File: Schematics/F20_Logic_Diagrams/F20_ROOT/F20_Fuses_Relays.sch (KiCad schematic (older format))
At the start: 11 parts, among them K1 MicroRelay, K2 MicroRelay, K3 MicroRelay, K4 MicroRelay, K5 MicroRelay

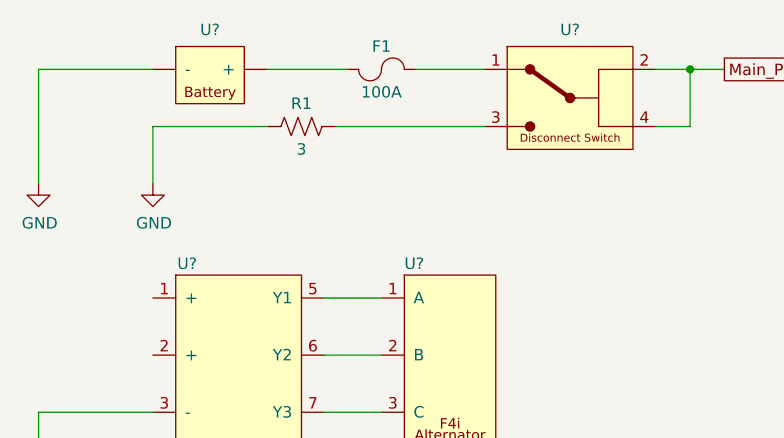
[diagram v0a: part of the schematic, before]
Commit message: Added Driver Display schematic. Added relevant symbols.
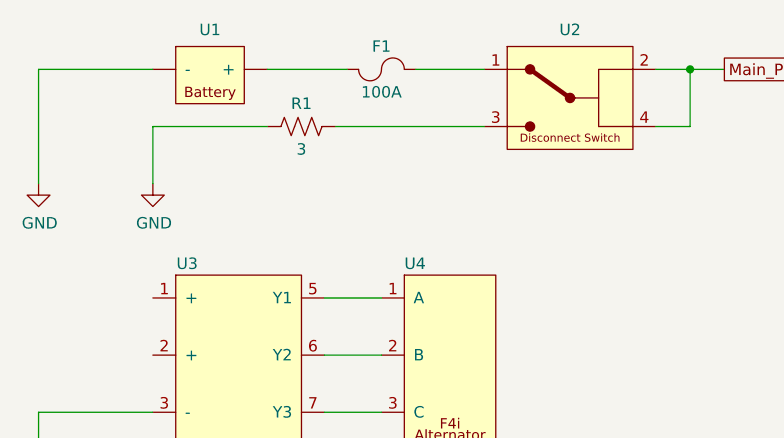
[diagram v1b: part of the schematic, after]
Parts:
- gave numbers to parts that had none: 4
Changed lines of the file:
@@
 EESchema Schematic File Version 4
-LIBS:F20_ROOT-cache
 EELAYER 30 0
 EELAYER END
 $Descr A 11000 8500
 encoding utf-8
-Sheet 2 4
+Sheet 2 5
 Title "Fuses and Relays"
 Date ""
@@
 	7250 1300 7250 2050
 $Comp
-L FSAE_Library:Rectifier U?
+L FSAE_Library:Rectifier U3
 U 1 1 5E21334A
 P 1500 2500
-F 0 "U?" H 1650 2650 50  0000 C CNN
+F 0 "U3" H 1650 2650 50  0000 C CNN
 F 1 "Rectifier" H 1750 2650 50  0001 C CNN
 F 2 "" H 2000 3000 50  0001 C CNN
@@
 $EndComp
 $Comp
-L FSAE_Library:Alternator U?
+L FSAE_Library:Alternator U4
 U 1 1 5E21541A
 P 2500 2500
-F 0 "U?" H 2600 2650 50  0000 L CNN
+F 0 "U4" H 2600 2650 50  0000 L CNN
 F 1 "Alternator" H 2800 2650 50  0001 C CNN
 F 2 "" H 2800 2650 50  0001 C CNN
@@
 Connection ~ 1000 3250
 $Comp
-L FSAE_Library:Battery U?
+L FSAE_Library:Battery U1
 U 1 1 5E233AF7
 P 2000 1500
-F 0 "U?" H 1750 1673 50  0000 C CNN
+F 0 "U1" H 1750 1673 50  0000 C CNN
 F 1 "Battery" H 1750 1650 50  0001 C CNN
 F 2 "" H 1750 1650 50  0001 C CNN
@@
 	1000 1500 1500 1500
 $Comp
-L FSAE_Library:Cutoff_Switch U?
+L FSAE_Library:Cutoff_Switch U2
 U 1 1 5E237569
 P 2950 1500
-F 0 "U?" H 3325 1673 50  0000 C CNN
+F 0 "U2" H 3325 1673 50  0000 C CNN
 F 1 "Cutoff_Switch" H 3300 1650 50  0001 C CNN
 F 2 "" H 3300 1650 50  0001 C CNN

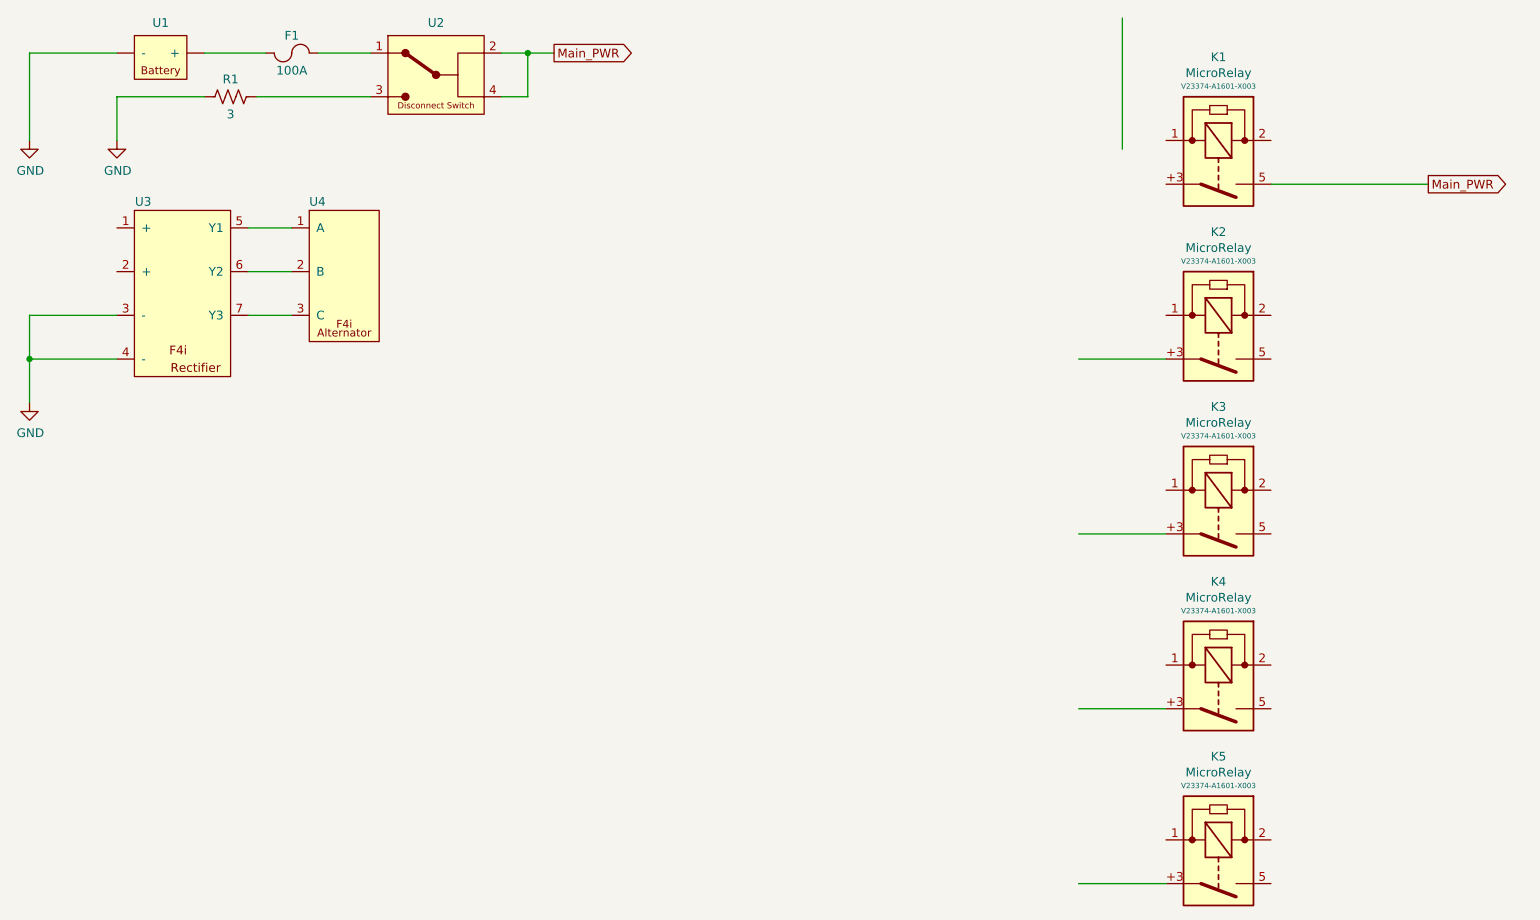
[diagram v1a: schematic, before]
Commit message: Added Brakes logic diagram draft, finished charging/starting schematic portion, added relevant library parts, updated README.
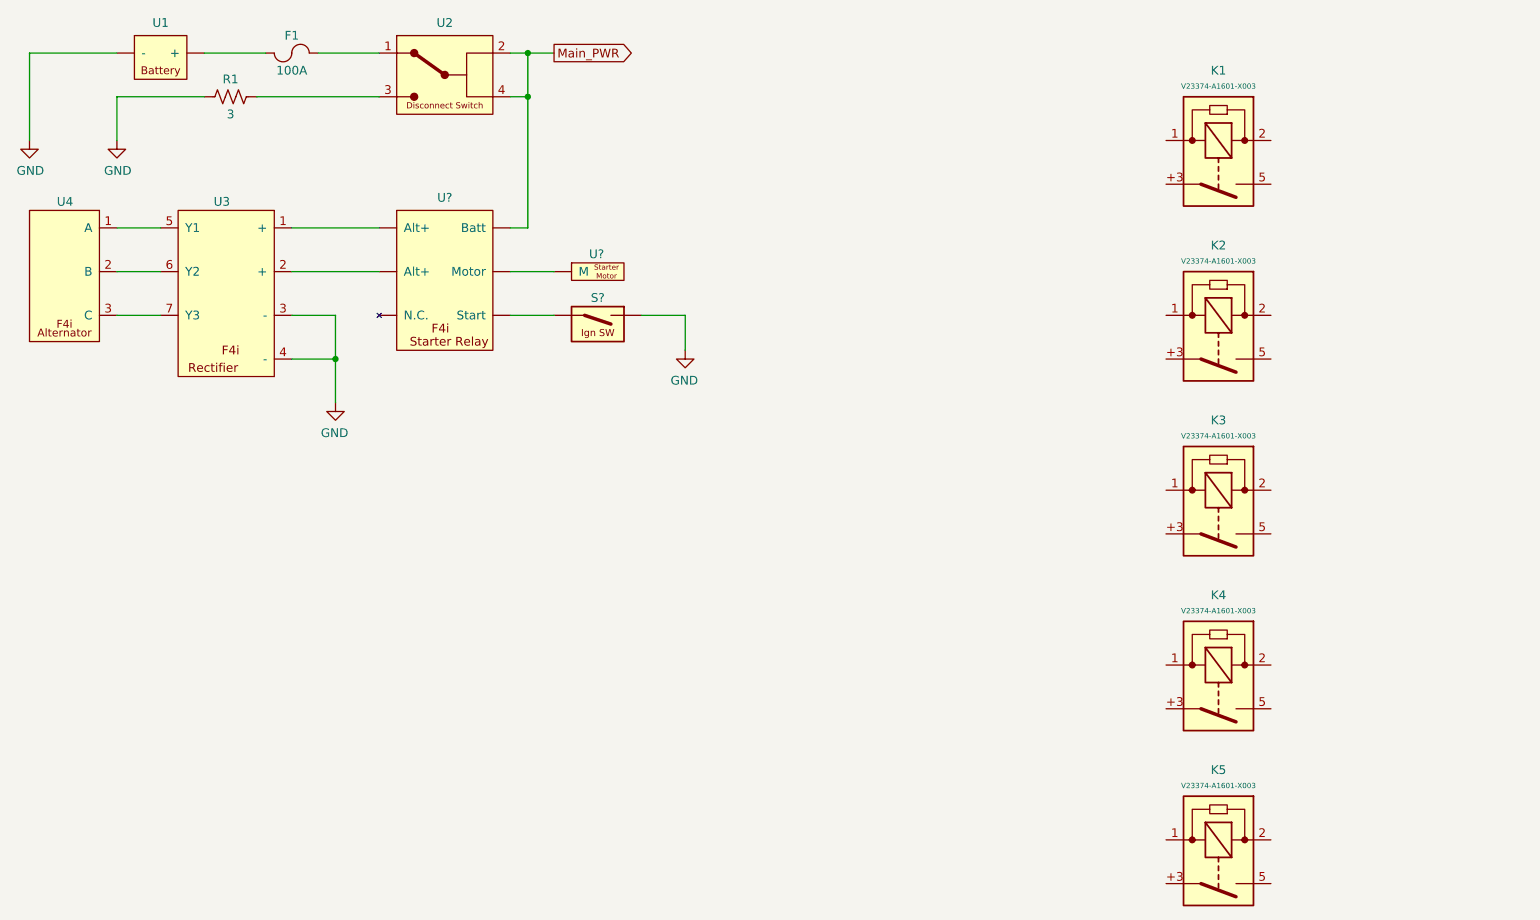
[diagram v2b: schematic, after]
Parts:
- added S?: Ignition_SW, symbol FSAE_Library:Ignition_SW
- added U?: Starter_Relay, symbol FSAE_Library:Starter_Relay
- added U?: Starter_Motor, symbol FSAE_Library:Starter_Motor
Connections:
- wire segments 24 -> 26
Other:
- moved on the sheet: U2, U3, U4
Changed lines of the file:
@@
 EESchema Schematic File Version 4
+LIBS:F20_ROOT-cache
 EELAYER 30 0
 EELAYER END
 $Descr A 11000 8500
 encoding utf-8
-Sheet 2 5
+Sheet 2 6
 Title "Fuses and Relays"
-Date ""
+Date "2020-01-28"
 Rev "A"
 Comp "F20"
@@
 U 1 1 5E20642A
 P 7500 2000
-F 0 "K1" H 7800 2477 50  0000 C CNN
-F 1 "MicroRelay" H 7800 2386 50  0000 C CNN
+F 0 "K1" H 7800 2400 50  0000 C CNN
+F 1 "MicroRelay" H 7800 2386 50  0001 C CNN
 F 2 "" H 7600 1450 50  0001 L CNN
 F 3 "https://www.waytekwire.com/item/75530/MICRO-RELAY-M3-12V-SPST-30A/" V 7800 1800 50  0001 C CNN
@@
 U 1 1 5E207459
 P 7500 3000
-F 0 "K2" H 7800 3477 50  0000 C CNN
-F 1 "MicroRelay" H 7800 3386 50  0000 C CNN
+F 0 "K2" H 7800 3400 50  0000 C CNN
+F 1 "MicroRelay" H 7800 3386 50  0001 C CNN
 F 2 "" H 7600 2450 50  0001 L CNN
 F 3 "https://www.waytekwire.com/item/75530/MICRO-RELAY-M3-12V-SPST-30A/" V 7800 2800 50  0001 C CNN
@@
 U 1 1 5E2083D6
 P 7500 4000
-F 0 "K3" H 7800 4477 50  0000 C CNN
-F 1 "MicroRelay" H 7800 4386 50  0000 C CNN
+F 0 "K3" H 7800 4400 50  0000 C CNN
+F 1 "MicroRelay" H 7800 4386 50  0001 C CNN
 F 2 "" H 7600 3450 50  0001 L CNN
 F 3 "https://www.waytekwire.com/item/75530/MICRO-RELAY-M3-12V-SPST-30A/" V 7800 3800 50  0001 C CNN
@@
 U 1 1 5E20AC84
 P 7500 5000
-F 0 "K4" H 7800 5477 50  0000 C CNN
-F 1 "MicroRelay" H 7800 5386 50  0000 C CNN
+F 0 "K4" H 7800 5400 50  0000 C CNN
+F 1 "MicroRelay" H 7800 5386 50  0001 C CNN
 F 2 "" H 7600 4450 50  0001 L CNN
 F 3 "https://www.waytekwire.com/item/75530/MICRO-RELAY-M3-12V-SPST-30A/" V 7800 4800 50  0001 C CNN
@@
 U 1 1 5E20B3C7
 P 7500 6000
-F 0 "K5" H 7800 6477 50  0000 C CNN
-F 1 "MicroRelay" H 7800 6386 50  0000 C CNN
+F 0 "K5" H 7800 6400 50  0000 C CNN
+F 1 "MicroRelay" H 7800 6386 50  0001 C CNN
 F 2 "" H 7600 5450 50  0001 L CNN
 F 3 "https://www.waytekwire.com/item/75530/MICRO-RELAY-M3-12V-SPST-30A/" V 7800 5800 50  0001 C CNN
@@
 	1    0    0    -1
 $EndComp
-Wire Wire Line
-	7500 6250 7000 6250
-Wire Wire Line
-	7000 5250 7500 5250
-Wire Wire Line
-	7000 4250 7500 4250
-Wire Wire Line
-	7000 3250 7500 3250
-Text GLabel 9000 2250 2    50   Output ~ 0
-Main_PWR
-Wire Wire Line
-	9000 2250 8100 2250
 Text GLabel 4000 1500 2    50   Output ~ 0
 Main_PWR
-Wire Wire Line
-	7250 1300 7250 2050
-$Comp
-L FSAE_Library:Rectifier U3
-U 1 1 5E21334A
-P 1500 2500
-F 0 "U3" H 1650 2650 50  0000 C CNN
-F 1 "Rectifier" H 1750 2650 50  0001 C CNN
-F 2 "" H 2000 3000 50  0001 C CNN
-F 3 "" H 2000 3000 50  0001 C CNN
-	1    1500 2500
-	1    0    0    -1
-$EndComp
-$Comp
-L FSAE_Library:Alternator U4
-U 1 1 5E21541A
-P 2500 2500
-F 0 "U4" H 2600 2650 50  0000 L CNN
-F 1 "Alternator" H 2800 2650 50  0001 C CNN
-F 2 "" H 2800 2650 50  0001 C CNN
-F 3 "" H 2800 2650 50  0001 C CNN
-	1    2500 2500
-	1    0    0    -1
-$EndComp
-Wire Wire Line
-	2250 2500 2500 2500
-Wire Wire Line
-	2250 2750 2500 2750
-Wire Wire Line
-	2250 3000 2500 3000
-$Comp
-L power:GND #PWR?
-U 1 1 5E2174D8
-P 1000 3500
-F 0 "#PWR?" H 1000 3250 50  0001 C CNN
-F 1 "GND" H 1005 3327 50  0000 C CNN
-F 2 "" H 1000 3500 50  0001 C CNN
-F 3 "" H 1000 3500 50  0001 C CNN
-	1    1000 3500
-	1    0    0    -1
-$EndComp
-Wire Wire Line
-	1000 3500 1000 3250
-Wire Wire Line
-	1000 3250 1500 3250
-Wire Wire Line
-	1000 3250 1000 3000
-Wire Wire Line
-	1000 3000 1500 3000
-Connection ~ 1000 3250
 $Comp
 L FSAE_Library:Battery U1
@@
 L FSAE_Library:Cutoff_Switch U2
 U 1 1 5E237569
-P 2950 1500
-F 0 "U2" H 3325 1673 50  0000 C CNN
-F 1 "Cutoff_Switch" H 3300 1650 50  0001 C CNN
-F 2 "" H 3300 1650 50  0001 C CNN
-F 3 "" H 3300 1650 50  0001 C CNN
-	1    2950 1500
-	1    0    0    -1
-$EndComp
-Wire Wire Line
-	2300 1750 2950 1750
+P 3000 1500
+F 0 "U2" H 3375 1673 50  0000 C CNN
+F 1 "Cutoff_Switch" H 3350 1650 50  0001 C CNN
+F 2 "" H 3350 1650 50  0001 C CNN
+F 3 "" H 3350 1650 50  0001 C CNN
+	1    3000 1500
+	1    0    0    -1
+$EndComp
+Wire Wire Line
+	2300 1750 3000 1750
 $Comp
 L power:GND #PWR?
@@
 	2000 1500 2350 1500
 Wire Wire Line
-	2650 1500 2950 1500
+	2650 1500 3000 1500
 $Comp
 L FSAE_Library:Fuse F1
@@
 $EndComp
 Wire Wire Line
-	3700 1500 3850 1500
-Wire Wire Line
-	3700 1750 3850 1750
+	3750 1500 3850 1500
+Wire Wire Line
+	3750 1750 3850 1750
 Wire Wire Line
 	3850 1750 3850 1500
@@
 Wire Wire Line
 	3850 1500 4000 1500
+Wire Wire Line
+	2750 3000 2500 3000
+Wire Wire Line
+	2750 3250 2500 3250
+$Comp
+L power:GND #PWR?
+U 1 1 5E2174D8
+P 2750 3500
+F 0 "#PWR?" H 2750 3250 50  0001 C CNN
+F 1 "GND" H 2755 3327 50  0000 C CNN
+F 2 "" H 2750 3500 50  0001 C CNN
+F 3 "" H 2750 3500 50  0001 C CNN
+	1    2750 3500
+	-1   0    0    -1
+$EndComp
+Wire Wire Line
+	1750 3000 1500 3000
+Wire Wire Line
+	1750 2750 1500 2750
+Wire Wire Line
+	1750 2500 1500 2500
+$Comp
+L FSAE_Library:Alternator U4
+U 1 1 5E21541A
+P 1500 2500
+F 0 "U4" H 1750 2650 50  0000 L CNN
+F 1 "Alternator" H 1800 2650 50  0001 C CNN
+F 2 "" H 1800 2650 50  0001 C CNN
+F 3 "" H 1800 2650 50  0001 C CNN
+	1    1500 2500
+	-1   0    0    -1
+$EndComp
+$Comp
+L FSAE_Library:Rectifier U3
+U 1 1 5E21334A
+P 2500 2500
+F 0 "U3" H 2900 2650 50  0000 C CNN
+F 1 "Rectifier" H 2750 2650 50  0001 C CNN
+F 2 "" H 3000 3000 50  0001 C CNN
+F 3 "" H 3000 3000 50  0001 C CNN
+	1    2500 2500
+	-1   0    0    -1
+$EndComp
+$Comp
+L FSAE_Library:Starter_Relay U?
+U 1 1 5E3285A1
+P 3000 2500
+F 0 "U?" H 3375 2673 50  0000 C CNN
+F 1 "Starter_Relay" H 3250 2650 50  0001 C CNN
+F 2 "" H 3500 3000 50  0001 C CNN
+F 3 "" H 3500 3000 50  0001 C CNN
+	1    3000 2500
+	1    0    0    -1
+$EndComp
+Wire Wire Line
+	2500 2750 3000 2750
+Wire Wire Line
+	2500 2500 3000 2500
+Wire Wire Line
+	2750 3000 2750 3250
+Connection ~ 2750 3250
+Wire Wire Line
+	2750 3250 2750 3500
+Wire Wire Line
+	3750 3000 4000 3000
+$Comp
+L power:GND #PWR?
+U 1 1 5E330233
+P 4750 3200
+F 0 "#PWR?" H 4750 2950 50  0001 C CNN
+F 1 "GND" H 4755 3027 50  0000 C CNN
+F 2 "" H 4750 3200 50  0001 C CNN
+F 3 "" H 4750 3200 50  0001 C CNN
+	1    4750 3200
+	-1   0    0    -1
+$EndComp
+Wire Wire Line
+	3850 1750 3850 2500
+Wire Wire Line
+	3850 2500 3750 2500
+Connection ~ 3850 1750
+$Comp
+L FSAE_Library:Starter_Motor U?
+U 1 1 5E3347A8
+P 4000 2750
+F 0 "U?" H 4200 2850 50  0000 L CNN
+F 1 "Starter_Motor" H 4250 2900 50  0001 C CNN
+F 2 "" H 4250 2900 50  0001 C CNN
+F 3 "" H 4250 2900 50  0001 C CNN
+	1    4000 2750
+	1    0    0    -1
+$EndComp
+Wire Wire Line
+	4000 2750 3750 2750
+$Comp
+L FSAE_Library:Ignition_SW S?
+U 1 1 5E335D97
+P 4000 3000
+F 0 "S?" H 4250 3100 50  0000 C CNN
+F 1 "Ignition_SW" H 4075 3150 50  0001 L CNN
+F 2 "" H 4100 2700 50  0001 L CNN
+F 3 "" V 4300 3050 50  0001 C CNN
+F 4 "" H 4300 2825 30  0000 C CNN "PN"
+	1    4000 3000
+	1    0    0    -1
+$EndComp
+Wire Wire Line
+	4500 3000 4750 3000
+Wire Wire Line
+	4750 3000 4750 3200
 $EndSCHEMATC
